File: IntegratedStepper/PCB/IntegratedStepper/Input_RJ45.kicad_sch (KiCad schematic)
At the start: 1 part, among them J1 8P8C

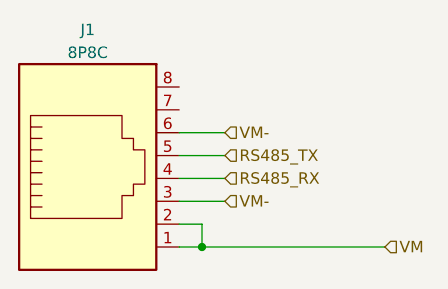
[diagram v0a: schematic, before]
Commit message: Add CAN circuit and edit bus from RS485 to CAN
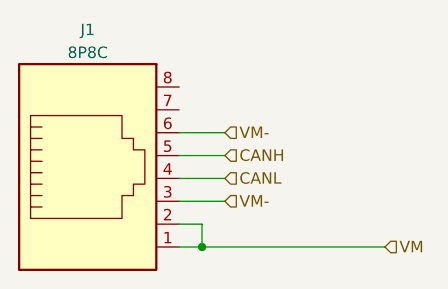
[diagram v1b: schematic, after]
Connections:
- net RS485_RX renamed CANL
- net RS485_TX renamed CANH
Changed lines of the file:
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@@
     (effects (font (size 1.27 1.27)) (justify left))
   )
-  (hierarchical_label "RS485_RX" (shape input) (at 151.13 85.09 0) (fields_autoplaced)
+  (hierarchical_label "CANL" (shape input) (at 151.13 85.09 0) (fields_autoplaced)
     (effects (font (size 1.27 1.27)) (justify left))
   )
-  (hierarchical_label "RS485_TX" (shape input) (at 151.13 82.55 0) (fields_autoplaced)
+  (hierarchical_label "CANH" (shape input) (at 151.13 82.55 0) (fields_autoplaced)
     (effects (font (size 1.27 1.27)) (justify left))
   )

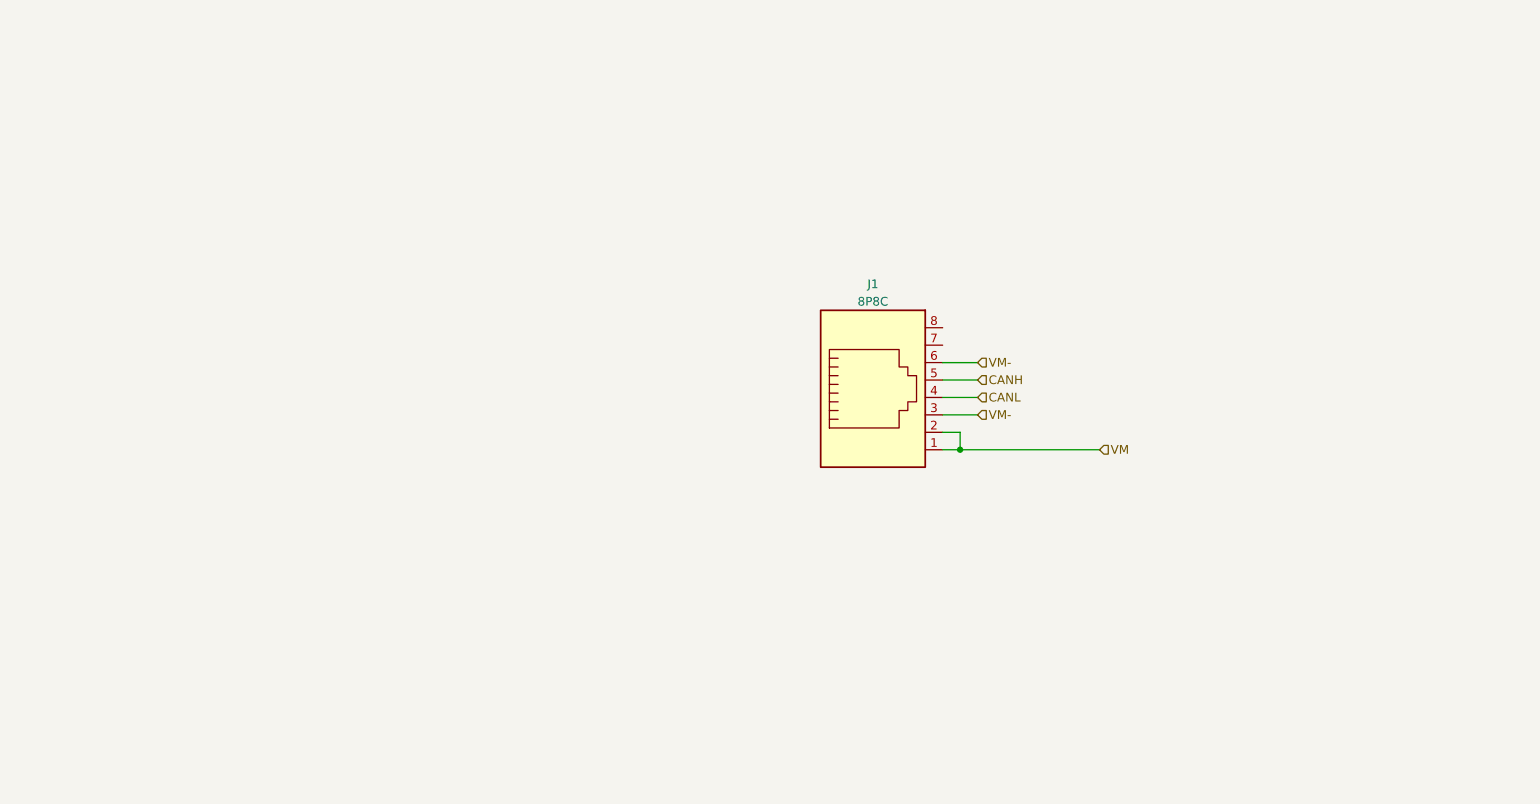
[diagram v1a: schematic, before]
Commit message: Update Integrated Stepper PCB with ESP sch and CAN sch
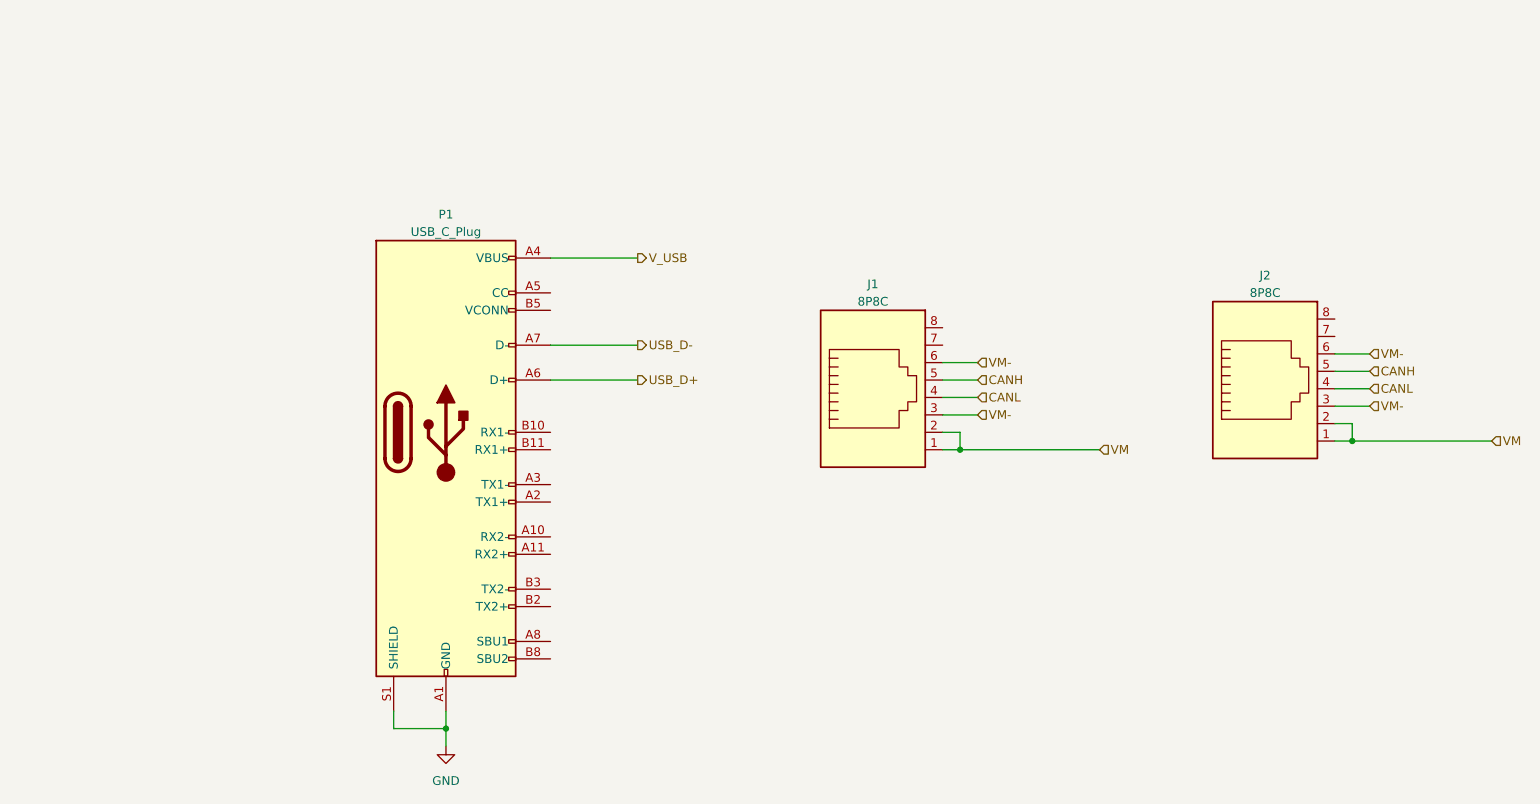
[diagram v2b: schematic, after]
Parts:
- added J2: 8P8C, symbol Connector:8P8C
- added P1: USB_C_Plug, Connector_USB:USB_C_Receptacle_GCT_USB4105-xx-A_16P_TopMnt_Horizontal, symbol Connector:USB_C_Plug
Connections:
- net CANH: now also J2.5
- net CANL: now also J2.4
- net VM: now also J2.1, J2.2
- net VM-: now also J2.3, J2.6
- new net GND: P1.A1 (GND), P1.A12 (GND), P1.B1 (GND), P1.B12 (GND), P1.S1 (SHIELD)
- new net USB_D+: P1.A6 (D+)
- new net USB_D-: P1.A7 (D-)
- new net V_USB: P1.A4 (VBUS), P1.A9 (VBUS), P1.B4 (VBUS), P1.B9 (VBUS)

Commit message: Update Integrated Stepper with inital PCB
This is going to be so hard :(
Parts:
- added J5: Conn_01x05_Socket, Connector_PinHeader_1.00mm:PinHeader_1x05_P1.00mm_Vertical_SMD_Pin1Left, symbol Connector:Conn_01x05_Socket
- added R23: 500, Resistor_SMD:R_0603_1608Metric, symbol Device:R_US
- added V3v1: LED, LED_SMD:LED_0603_1608Metric, symbol Device:LED
- J1, J2: footprint (none) -> Connector_RJ:RJ45_Amphenol_54602-x08_Horizontal
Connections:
- net GND: now also J5.5 (Pin_5), R23.1
- net V_USB: now also J5.1 (Pin_1), V3v1.2 (A)
- new net: R23.2, V3v1.1 (K)
- new net ENC+: J5.3 (Pin_3)
- new net ENC-: J5.2 (Pin_2)
- new net ENC_IND: J5.4 (Pin_4)

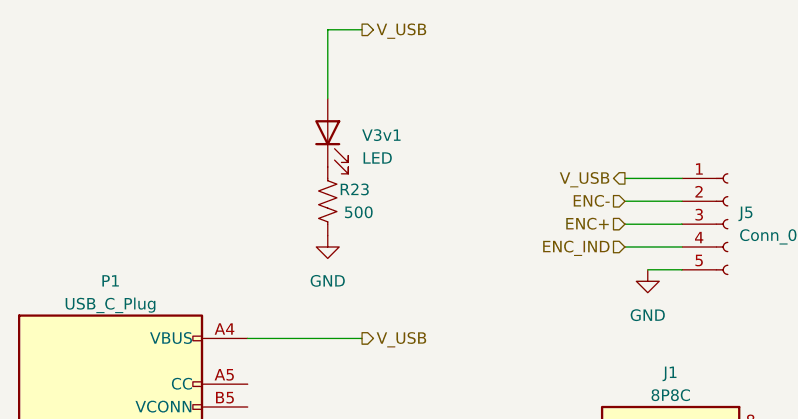
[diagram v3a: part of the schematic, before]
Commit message: Add intermediate layout + routing to integrated stepper
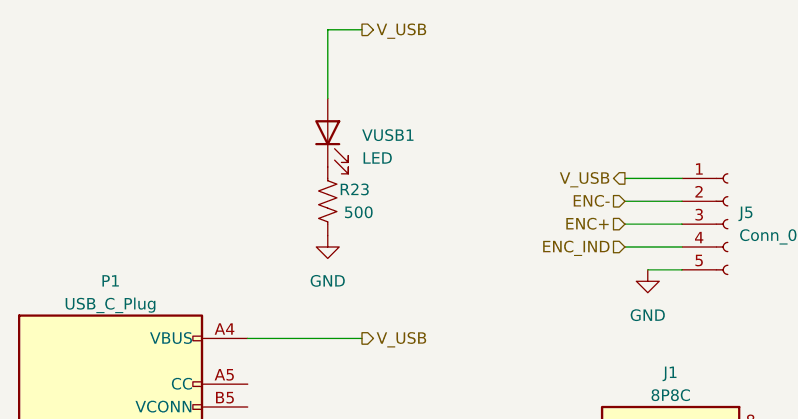
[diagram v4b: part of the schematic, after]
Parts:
- P1: footprint Connector_USB:USB_C_Receptacle_GCT_USB4105-xx-A_16P_TopMnt_Horizontal -> Connector_USB:USB_C_Receptacle_G-Switch_GT-USB-7051x
- renumbered V3v1 to VUSB1
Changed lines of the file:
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@@
 		(dnp no)
 		(fields_autoplaced yes)
-		(property "Reference" "V3v1"
+		(property "Reference" "VUSB1"
 			(at 101.6 42.2274 90)
 			(effects
@@
 			(project "IntegratedStepper"
 				(path "/ab592993-dafc-411a-b466-8e8425f43767/1bafc6f7-07ea-452b-8b4f-66f8063c8934"
-					(reference "V3v1")
+					(reference "VUSB1")
 					(unit 1)
 				)
@@
 			)
 		)
-		(property "Footprint" "Connector_USB:USB_C_Receptacle_GCT_USB4105-xx-A_16P_TopMnt_Horizontal"
+		(property "Footprint" "Connector_USB:USB_C_Receptacle_G-Switch_GT-USB-7051x"
 			(at 77.47 90.17 0)
 			(effects

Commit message: Add final layout + 3D models
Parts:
- removed P1: USB_C_Plug, Connector_USB:USB_C_Receptacle_G-Switch_GT-USB-7051x, symbol Connector:USB_C_Plug
- added USBC1: TYPE-C 3.1_C168690, easyeda2kicad:USB-C-SMD_TYPE-C-USB-3, symbol easyeda2kicad:TYPE-C3.1_C168690
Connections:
- net GND: now also USBC1.0, USBC1.A1, USBC1.A12, USBC1.B1, USBC1.B12
- net USB_D+: now also USBC1.A6, USBC1.B6
- net USB_D-: now also USBC1.A7, USBC1.B7
- net V_USB: now also USBC1.A4, USBC1.A9, USBC1.B4, USBC1.B9

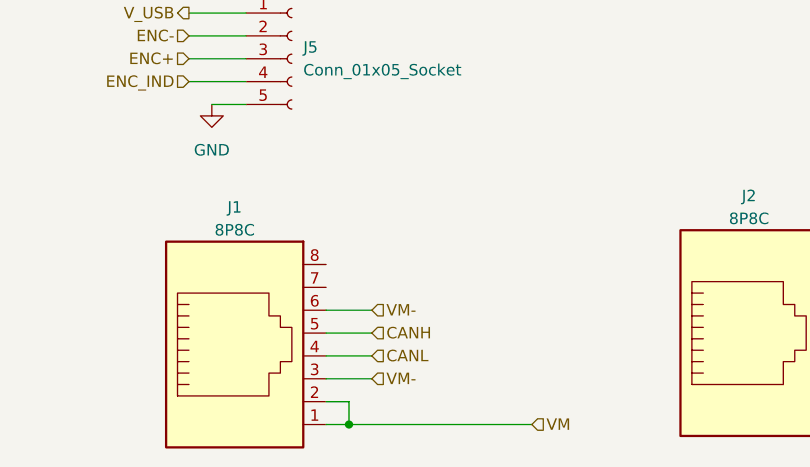
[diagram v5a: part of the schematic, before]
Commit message: add changes for instock parts
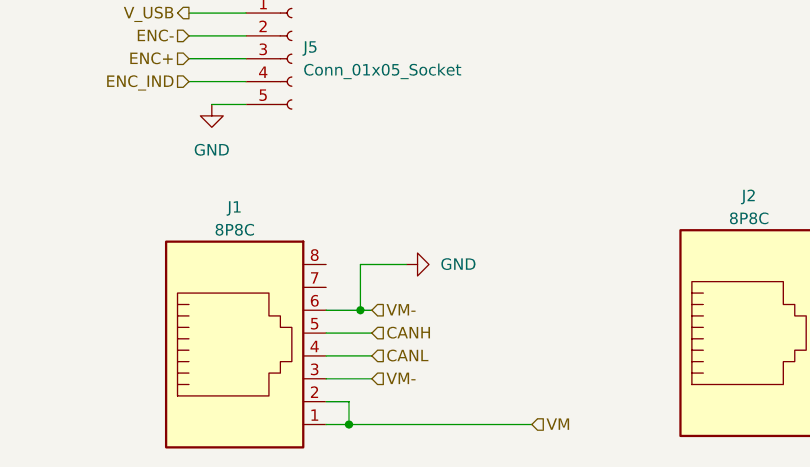
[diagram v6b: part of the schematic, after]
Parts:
- J1, J2: footprint Connector_RJ:RJ45_Amphenol_54602-x08_Horizontal -> easyeda2kicad:RJ45-TH_KH-RJ45-58-8P8C; LCSC (none) -> C2683360; LCSC Part (none) -> C2683360; LCSC Part Number (none) -> C2683360
- R23: LCSC (none) -> C2989147; LCSC Part (none) -> C2989147; LCSC Part Number (none) -> C2989147
- USBC1: LCSC (none) -> C168690; LCSC Part Number (none) -> C168690
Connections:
- net VM- is gone; now on net GND: J1.3, J1.6, J2.3, J2.6
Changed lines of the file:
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@@
 		(color 0 0 0 0)
 	)
+	(junction
+		(at 149.86 80.01)
+		(diameter 0)
+		(color 0 0 0 0)
+	)
 	(wire
 		(pts
@@
 	(wire
 		(pts
+			(xy 154.94 74.93) (xy 149.86 74.93)
+		)
+		(stroke
+			(width 0)
+			(type default)
+		)
+	)
+	(wire
+		(pts
 			(xy 34.29 76.2) (xy 36.83 76.2)
 		)
@@
 	(wire
 		(pts
+			(xy 149.86 80.01) (xy 151.13 80.01)
+		)
+		(stroke
+			(width 0)
+			(type default)
+		)
+	)
+	(wire
+		(pts
 			(xy 148.59 90.17) (xy 148.59 92.71)
 		)
@@
 	(wire
 		(pts
+			(xy 149.86 74.93) (xy 149.86 80.01)
+		)
+		(stroke
+			(width 0)
+			(type default)
+		)
+	)
+	(wire
+		(pts
 			(xy 130.81 46.99) (xy 137.16 46.99)
 		)
@@
 	(wire
 		(pts
-			(xy 146.05 80.01) (xy 151.13 80.01)
+			(xy 146.05 80.01) (xy 149.86 80.01)
 		)
 		(stroke
@@
 			)
 		)
-		(property "Footprint" "Connector_RJ:RJ45_Amphenol_54602-x08_Horizontal"
+		(property "Footprint" "easyeda2kicad:RJ45-TH_KH-RJ45-58-8P8C"
 			(at 135.89 84.455 90)
 			(effects
@@
 		)
 		(property "Description" ""
+			(at 135.89 85.09 0)
+			(effects
+				(font
+					(size 1.27 1.27)
+				)
+				(hide yes)
+			)
+		)
+		(property "LCSC" "C2683360"
+			(at 135.89 85.09 0)
+			(effects
+				(font
+					(size 1.27 1.27)
+				)
+				(hide yes)
+			)
+		)
+		(property "LCSC Part" "C2683360"
+			(at 135.89 85.09 0)
+			(effects
+				(font
+					(size 1.27 1.27)
+				)
+				(hide yes)
+			)
+		)
+		(property "LCSC Part Number" "C2683360"
 			(at 135.89 85.09 0)
 			(effects
@@
 	)
 	(symbol
+		(lib_id "power:GND")
+		(at 154.94 74.93 90)
+		(unit 1)
+		(exclude_from_sim no)
+		(in_bom yes)
+		(on_board yes)
+		(dnp no)
+		(fields_autoplaced yes)
+		(property "Reference" "#PWR044"
+			(at 161.29 74.93 0)
+			(effects
+				(font
+					(size 1.27 1.27)
+				)
+				(hide yes)
+			)
+		)
+		(property "Value" "GND"
+			(at 158.75 74.9299 90)
+			(effects
+				(font
+					(size 1.27 1.27)
+				)
+				(justify right)
+			)
+		)
+		(property "Footprint" ""
+			(at 154.94 74.93 0)
+			(effects
+				(font
+					(size 1.27 1.27)
+				)
+				(hide yes)
+			)
+		)
+		(property "Datasheet" ""
+			(at 154.94 74.93 0)
+			(effects
+				(font
+					(size 1.27 1.27)
+				)
+				(hide yes)
+			)
+		)
+		(property "Description" ""
+			(at 154.94 74.93 0)
+			(effects
+				(font
+					(size 1.27 1.27)
+				)
+				(hide yes)
+			)
+		)
+		(pin "1"
+		)
+		(instances
+			(project "IntegratedStepper"
+				(path "/ab592993-dafc-411a-b466-8e8425f43767/1bafc6f7-07ea-452b-8b4f-66f8063c8934"
+					(reference "#PWR044")
+					(unit 1)
+				)
+			)
+		)
+	)
+	(symbol
 		(lib_id "Connector:8P8C")
 		(at 193.04 83.82 0)
@@
 			)
 		)
-		(property "Footprint" "Connector_RJ:RJ45_Amphenol_54602-x08_Horizontal"
+		(property "Footprint" "easyeda2kicad:RJ45-TH_KH-RJ45-58-8P8C"
 			(at 193.04 83.185 90)
 			(effects
@@
 		)
 		(property "Description" ""
+			(at 193.04 83.82 0)
+			(effects
+				(font
+					(size 1.27 1.27)
+				)
+				(hide yes)
+			)
+		)
+		(property "LCSC" "C2683360"
+			(at 193.04 83.82 0)
+			(effects
+				(font
+					(size 1.27 1.27)
+				)
+				(hide yes)
+			)
+		)
+		(property "LCSC Part" "C2683360"
+			(at 193.04 83.82 0)
+			(effects
+				(font
+					(size 1.27 1.27)
+				)
+				(hide yes)
+			)
+		)
+		(property "LCSC Part Number" "C2683360"
 			(at 193.04 83.82 0)
 			(effects
@@
 			)
 		)
+		(property "LCSC" "C2989147"
+			(at 97.79 49.53 0)
+			(effects
+				(font
+					(size 1.27 1.27)
+				)
+				(hide yes)
+			)
+		)
+		(property "LCSC Part" "C2989147"
+			(at 97.79 49.53 0)
+			(effects
+				(font
+					(size 1.27 1.27)
+				)
+				(hide yes)
+			)
+		)
+		(property "LCSC Part Number" "C2989147"
+			(at 97.79 49.53 0)
+			(effects
+				(font
+					(size 1.27 1.27)
+				)
+				(hide yes)
+			)
+		)
 		(pin "2"
 		)
@@
 			(effects
 				(font
+					(size 1.27 1.27)
+				)
+				(hide yes)
+			)
+		)
+		(property "LCSC" "C168690"
+			(at 35.56 54.61 0)
+			(effects
+				(font
+					(size 1.27 1.27)
+				)
+				(hide yes)
+			)
+		)
+		(property "LCSC Part Number" "C168690"
+			(at 35.56 54.61 0)
+			(effects
+				(font

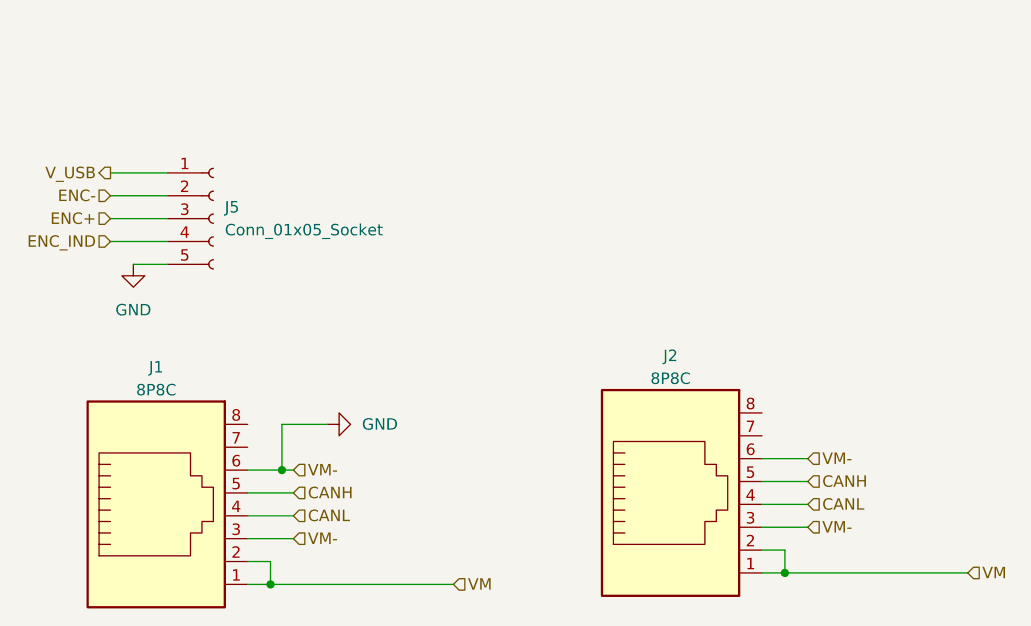
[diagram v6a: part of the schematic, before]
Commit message: update with more in stock parts
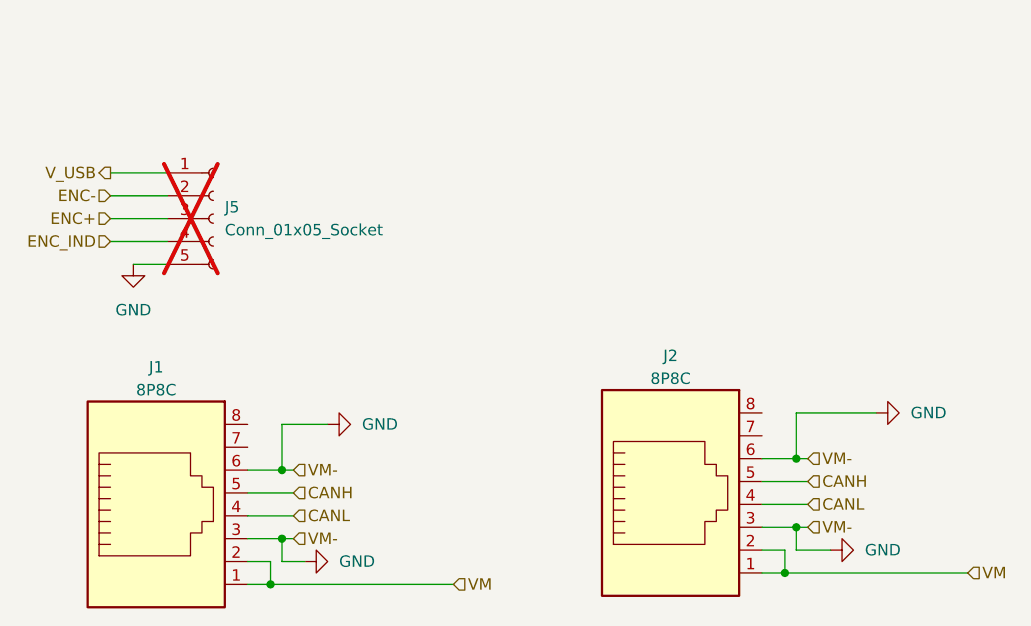
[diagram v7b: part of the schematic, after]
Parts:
- J5: now not fitted
- VUSB1: LCSC (none) -> C965804; LCSC Part (none) -> C965804; LCSC Part Number (none) -> C965804

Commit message: add 3D model
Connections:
- net V_USB: no longer J5.1 (Pin_1)
- new net 3V3_VCC: J5.1 (Pin_1)
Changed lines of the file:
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@@
 		)
 	)
-	(hierarchical_label "V_USB"
+	(hierarchical_label "3V3_VCC"
 		(shape output)
 		(at 130.81 46.99 180)
@@
 		)
 		(property "Intersheetrefs" "${INTERSHEET_REFS}"
-			(at 122.7211 46.99 0)
+			(at 120.4835 46.99 0)
 			(effects
 				(font
